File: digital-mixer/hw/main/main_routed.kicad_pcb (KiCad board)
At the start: 2 copper layers, 114 x 127.9 mm, 184 parts, among them J1 GCT USB4085, J10 MIDI OUT SJ-43514-SMT, J2 LiPo 1S 3000 mAh (з платою за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, J3 IN1 SJ-43514-SMT, J4 IN2 SJ-43514-SMT, J5 IN3 SJ-43514-SMT, J6 IN4 SJ-43514-SMT, J7 MAIN OUT SJ-43514-SMT, J8 AUX OUT SJ-43514-SMT, J9 PHONES SJ-43514-SMT, Q1 AO3401A, SW1 Power 7x7 DPDT self-lock, SW10 EC11 ch3.1, SW11 EC11 ch3.2, SW12 EC11 ch3.3, SW13 Mute 3 TSF-1266, SW14 EC11 ch4.1, SW15 EC11 ch4.2, SW16 EC11 ch4.3, SW17 Mute 4 TSF-1266, SW18 EC11 master, SW19 FX1 TSF-1266, SW2 EC11 ch1.1, SW20 FX2 TSF-1266, SW21 AUX TSF-1266, SW22 CUE TSF-1266, SW23 SHIFT TSF-1266, SW3 EC11 ch1.2, SW4 EC11 ch1.3, SW5 Mute 1 TSF-1266, SW6 EC11 ch2.1, SW7 EC11 ch2.2, SW8 EC11 ch2.3, SW9 Mute 2 TSF-1266, U1 Teensy 4.1, U10 PCM5102A, U11 TPA6132A2, U12 MCP23017-E/SO, U13 MCP23017-E/SO, U2 USBLC6-2SC6, U3 TP4056, U4 TPS63802, U5 LP5907MFX-3.3, U6 PCM1865, U7 PCM1865, U8 PCM5102A, U9 PCM5102A

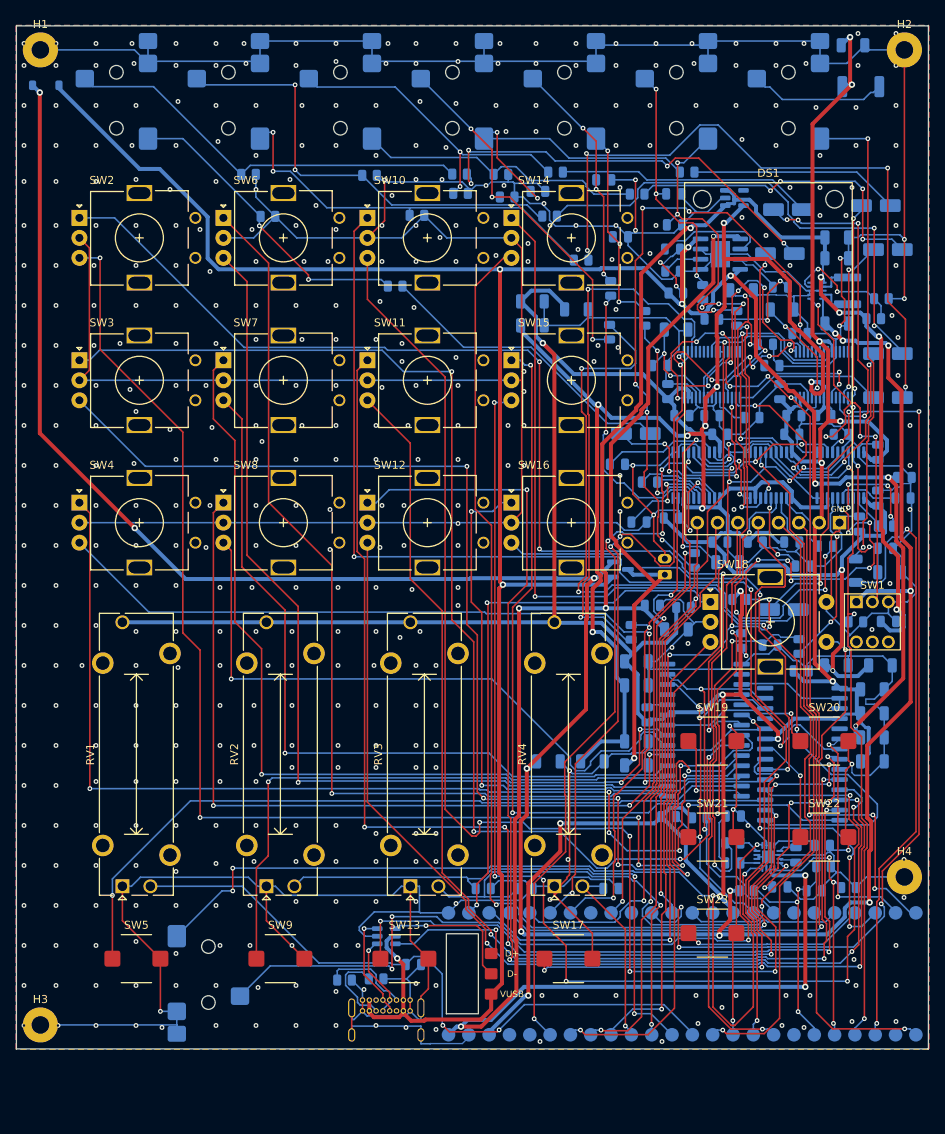
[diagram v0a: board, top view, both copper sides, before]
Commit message: digital-mixer: компоновка C (DM25-DM30), SMD-енкодери, USB4110, розводка 0 помилок
- компоновка C: колонки каналів на одних осях, ON / дисплей / MASTER в один ряд,
  Teensy у передньому правому куті, виходи на правому торці, M2 у чотирьох кутах
- EC12SY SMD з кнопками (DM26) + третій MCP23017; кнопку CUE прибрано (DM28)
- кнопка живлення 5,8 мм SMD (DM27), USB-C GCT USB4110 SMD (DM30), JST PH SMD
- 33 Ω на тактах I2S / TDM (DM29); такти 60-73 мм замість ~110
- 3D-моделі для всіх власних і стокових footprint без моделі (hw/lib/gen_3d.py)
- common: route_pcb --hole-keep, rip_near.py, параметри проєкту в kisch
- DRC: 0 порушень, 0 нез'єднаних, 0 розбіжностей зі схемою; ERC 0

Co-Authored-By: Claude Opus 5.5 <noreply@anthropic.com>
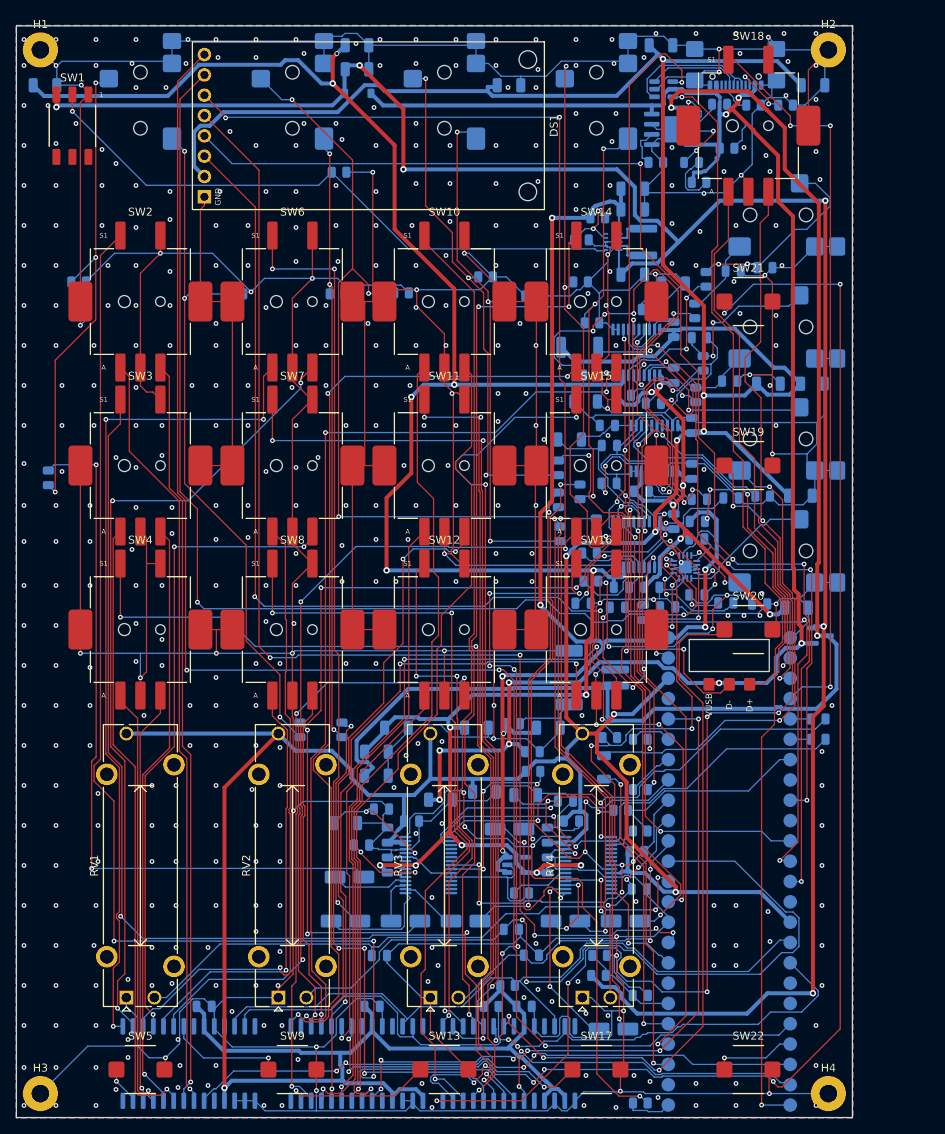
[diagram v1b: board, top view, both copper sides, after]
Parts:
- removed SW23: SHIFT TSF-1266, pocket-digital:SW_TSF-1266_6x6mm_SMD
- added C82: 10u, Capacitor_SMD:C_1206_3216Metric, B.Cu at (119.6, 27.4)
- added R44: 470, Resistor_SMD:R_0805_2012Metric, B.Cu at (105.8, 62.2)
- added R45: 470, Resistor_SMD:R_0805_2012Metric, B.Cu at (91.6, 85.9)
- added R46: 470, Resistor_SMD:R_0805_2012Metric, B.Cu at (91.8, 89.4)
- added R47: 33 0.5W, Resistor_SMD:R_2010_5025Metric, B.Cu at (90.4, 60.2)
- added R48: 10 0.25W, Resistor_SMD:R_1206_3216Metric, B.Cu at (93.4, 112.7)
- added U14: MCP23017-E/SO, Package_SO:SOIC-28W_7.5x17.9mm_P1.27mm, B.Cu at (81.6, 149.7)
- C81: value 10u -> 100n; footprint Capacitor_SMD:C_1206_3216Metric -> Capacitor_SMD:C_0805_2012Metric
- J1: value GCT USB4085 -> GCT USB4110-GF-A; footprint Connector_USB:USB_C_Receptacle_GCT_USB4085 -> Connector_USB:USB_C_Receptacle_GCT_USB4110
- J2: footprint Connector_JST:JST_PH_B2B-PH-K_1x02_P2.00mm_Vertical -> Connector_JST:JST_PH_S2B-PH-SM4-TB_1x02-1MP_P2.00mm_Horizontal
- R10: value 5.1k -> 10k
- R11: value 2.4k -> 10k
- R12, R13: value 1k -> 100k
- R14: value 100k -> 5.1k
- R15: value 665k -> 5.1k
- R16: value 91k -> 2.4k
- R17, R18: value 100k -> 1k
- R19, R23, R25, R32, R34: value 10k -> 100k
- R20: value 100k -> 665k
- R21: value 10k -> 91k
- R24, R33: value 100k -> 10k
- R26, R35: value 33 -> 10k
- R31, R7, R8: value 100k -> 33
- R36, R38: value 470 -> 100k
- R37, R39: value 470 -> 10k
- R40: value 470 -> 33
- R42: value 33 0.5W -> 470; footprint Resistor_SMD:R_2010_5025Metric -> Resistor_SMD:R_0805_2012Metric
- R43: value 10 0.25W -> 470; footprint Resistor_SMD:R_1206_3216Metric -> Resistor_SMD:R_0805_2012Metric
- R5, R6: value 10k -> 33
- R9: value 5.1k -> 33
- SW1: value Power 7x7 DPDT self-lock -> Power 5.8mm DPDT self-lock SMD; footprint pocket-digital:SW_Push_Latching_DPDT_7x7mm -> pocket-digital:SW_Push_Latching_DPDT_5.8mm_SMD
- SW10: value EC11 ch3.1 -> EC12SY ch3.1; footprint Rotary_Encoder:RotaryEncoder_Alps_EC11E_Vertical_H20mm -> pocket-digital:RotaryEncoder_EC12SY_SMD
- SW11: value EC11 ch3.2 -> EC12SY ch3.2; footprint Rotary_Encoder:RotaryEncoder_Alps_EC11E_Vertical_H20mm -> pocket-digital:RotaryEncoder_EC12SY_SMD
- SW12: value EC11 ch3.3 -> EC12SY ch3.3; footprint Rotary_Encoder:RotaryEncoder_Alps_EC11E_Vertical_H20mm -> pocket-digital:RotaryEncoder_EC12SY_SMD
- SW14: value EC11 ch4.1 -> EC12SY ch4.1; footprint Rotary_Encoder:RotaryEncoder_Alps_EC11E_Vertical_H20mm -> pocket-digital:RotaryEncoder_EC12SY_SMD
- SW15: value EC11 ch4.2 -> EC12SY ch4.2; footprint Rotary_Encoder:RotaryEncoder_Alps_EC11E_Vertical_H20mm -> pocket-digital:RotaryEncoder_EC12SY_SMD
- SW16: value EC11 ch4.3 -> EC12SY ch4.3; footprint Rotary_Encoder:RotaryEncoder_Alps_EC11E_Vertical_H20mm -> pocket-digital:RotaryEncoder_EC12SY_SMD
- SW18: value EC11 master -> EC12SY master; footprint Rotary_Encoder:RotaryEncoder_Alps_EC11E-Switch_Vertical_H20mm -> pocket-digital:RotaryEncoder_EC12SY_SMD
- SW2: value EC11 ch1.1 -> EC12SY ch1.1; footprint Rotary_Encoder:RotaryEncoder_Alps_EC11E_Vertical_H20mm -> pocket-digital:RotaryEncoder_EC12SY_SMD
- SW22: value CUE TSF-1266 -> SHIFT TSF-1266
- SW3: value EC11 ch1.2 -> EC12SY ch1.2; footprint Rotary_Encoder:RotaryEncoder_Alps_EC11E_Vertical_H20mm -> pocket-digital:RotaryEncoder_EC12SY_SMD
- SW4: value EC11 ch1.3 -> EC12SY ch1.3; footprint Rotary_Encoder:RotaryEncoder_Alps_EC11E_Vertical_H20mm -> pocket-digital:RotaryEncoder_EC12SY_SMD
- SW6: value EC11 ch2.1 -> EC12SY ch2.1; footprint Rotary_Encoder:RotaryEncoder_Alps_EC11E_Vertical_H20mm -> pocket-digital:RotaryEncoder_EC12SY_SMD
- SW7: value EC11 ch2.2 -> EC12SY ch2.2; footprint Rotary_Encoder:RotaryEncoder_Alps_EC11E_Vertical_H20mm -> pocket-digital:RotaryEncoder_EC12SY_SMD
- SW8: value EC11 ch2.3 -> EC12SY ch2.3; footprint Rotary_Encoder:RotaryEncoder_Alps_EC11E_Vertical_H20mm -> pocket-digital:RotaryEncoder_EC12SY_SMD
- moved J1 124.9 mm to (109.9, 23.7), turned to 0 degrees
- moved SW1 117.7 mm to (27.0, 32.5)
- moved U2 111.4 mm to (100.9, 27.9)
- moved C81 108.8 mm to (97.9, 127.9)
- moved J9 99.9 mm to (123.2, 85.6), turned to 180 degrees
- moved C13 94.7 mm to (61.6, 126.4)
- moved C52 94.2 mm to (62.6, 22.4)
- moved C14 94.2 mm to (61.1, 131.9)
- moved C24 93.1 mm to (88.6, 131.9)
- moved C25 91.2 mm to (96.1, 131.9)
- moved C26 90.4 mm to (81.6, 120.4)
- moved C6 89.8 mm to (62.6, 25.4)
- moved C15 88.4 mm to (76.1, 131.9)
- moved U5 87.7 mm to (82.5, 124.9)
- moved R13 83.3 mm to (92.9, 136.2)
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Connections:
- C77 pad 1: /FADER1 -> /+3V3
- C78 pad 1: /FADER2 -> /FADER1
- C79 pad 1: /FADER3 -> /FADER2
- C80 pad 1: /FADER4 -> /FADER3
- C81 pad 1: /+3V3 -> /FADER4
- R10 pad 1: /CC2 -> /DAC_XSMT
- R11 pad 1: /CHG_PROG -> /HP_EN
- R12 pad 1: /VBUS -> /VSYS
- R12 pad 2: /CHG_LED_RA -> /VBAT_SENSE
- R13 pad 1: /VBUS -> /VBAT_SENSE
- R13 pad 2: /CHG_LED_GA -> /GND
- R14 pad 1: /VBUS -> /CC1
- R15 pad 1: /+4V2 -> /CC2
- R15 pad 2: /BB_FB -> /GND
- R16 pad 1: /BB_FB -> /CHG_PROG
- R17 pad 1: /PWR_EN -> /VBUS
- R17 pad 2: /GND -> /CHG_LED_RA
- R18 pad 1: /IN1_T -> /VBUS
- R18 pad 2: /GND -> /CHG_LED_GA
- R19 pad 1: /IN1_T -> /VBUS
- R19 pad 2: /IN1_LS -> /GND
- R20 pad 1: /IN1_R -> /+4V2
- R20 pad 2: /GND -> /BB_FB
- R21 pad 1: /IN1_R -> /BB_FB
- R21 pad 2: /IN1_RS -> /GND
- R22 pad 1: /IN2_T -> /PWR_EN
- R23 pad 1: /IN2_T -> /IN1_T
- R23 pad 2: /IN2_LS -> /GND
- R24 pad 1: /IN2_R -> /IN1_T
- R24 pad 2: /GND -> /IN1_LS
- R25 pad 1: /IN2_R -> /IN1_R
- R25 pad 2: /IN2_RS -> /GND
- R26 pad 1: /ADC1_DOUT -> /IN1_R
- R26 pad 2: /ADC_DOUT -> /IN1_RS
- R27 pad 1: /IN3_T -> /IN2_T
- R28 pad 1: /IN3_T -> /IN2_T
- R28 pad 2: /IN3_LS -> /IN2_LS
- R29 pad 1: /IN3_R -> /IN2_R
- R30 pad 1: /IN3_R -> /IN2_R
- R30 pad 2: /IN3_RS -> /IN2_RS
- R31 pad 1: /IN4_T -> /ADC1_DOUT
- R31 pad 2: /GND -> /ADC_DOUT
- R32 pad 1: /IN4_T -> /IN3_T
- R32 pad 2: /IN4_LS -> /GND
- R33 pad 1: /IN4_R -> /IN3_T
- R33 pad 2: /GND -> /IN3_LS
- R34 pad 1: /IN4_R -> /IN3_R
- R34 pad 2: /IN4_RS -> /GND
- R35 pad 1: /ADC2_DOUT -> /IN3_R
- R35 pad 2: /ADC_DOUT -> /IN3_RS
- R36 pad 1: /MAIN_OL -> /IN4_T
- R36 pad 2: /MAIN_L -> /GND
- R37 pad 1: /MAIN_OR -> /IN4_T
- R37 pad 2: /MAIN_R -> /IN4_LS
- R38 pad 1: /AUX_OL -> /IN4_R
- R38 pad 2: /AUX_L -> /GND
- R39 pad 1: /AUX_OR -> /IN4_R
- R39 pad 2: /AUX_R -> /IN4_RS
- R40 pad 1: /CUE_OL -> /ADC2_DOUT
- R40 pad 2: /CUE_L -> /ADC_DOUT
- R41 pad 1: /CUE_OR -> /MAIN_OL
- R41 pad 2: /CUE_R -> /MAIN_L
- R42 pad 1: /+3V3 -> /MAIN_OR
- R42 pad 2: /MIDI_SRC -> /MAIN_R
- R43 pad 1: /MIDI_TX -> /AUX_OL
- R43 pad 2: /MIDI_SINK -> /AUX_L
- R5 pad 1: /DAC_XSMT -> /DAC_BCK_T
- R5 pad 2: /GND -> /DAC_BCK
- R6 pad 1: /HP_EN -> /DAC_LRCK_T
- R6 pad 2: /GND -> /DAC_LRCK
- R7 pad 1: /VSYS -> /ADC_BCK_T
- R7 pad 2: /VBAT_SENSE -> /ADC_BCK
- R8 pad 1: /VBAT_SENSE -> /ADC_LRCK_T
- R8 pad 2: /GND -> /ADC_LRCK
- R9 pad 1: /CC1 -> /ADC_MCLK_T
- R9 pad 2: /GND -> /ADC_MCLK
- SW1 pad 1: /VSYS -> /GND
- SW1 pad 3: /GND -> /VSYS
- SW10 pad MP: (no net) -> /GND
- SW11 pad MP: (no net) -> /GND
- SW12 pad MP: (no net) -> /GND
- SW14 pad MP: (no net) -> /GND
- SW15 pad MP: (no net) -> /GND
- SW16 pad MP: (no net) -> /GND
- SW18 pad MP: (no net) -> /GND
- SW2 pad MP: (no net) -> /GND
- SW22 pad 1: /BTN_CUE -> /BTN_SHIFT
- SW3 pad MP: (no net) -> /GND
- SW4 pad MP: (no net) -> /GND
- SW6 pad MP: (no net) -> /GND
- SW7 pad MP: (no net) -> /GND
- SW8 pad MP: (no net) -> /GND
- U1 pad 25: /ADC_MCLK -> /ADC_MCLK_T
- U1 pad 42: /DAC_LRCK -> /DAC_LRCK_T
- U1 pad 43: /DAC_BCK -> /DAC_BCK_T
- U1 pad 44: unconnected-(U1-22_A8_CTX1-Pad44) -> /MCP3_INT
- U1 pad 5: /ADC_LRCK -> /ADC_LRCK_T
- U1 pad 6: /ADC_BCK -> /ADC_BCK_T
- U12 pad 28: /BTN_FX1 -> unconnected-(U12-GPA7-Pad28)
- U12 pad 8: /BTN_FX2 -> unconnected-(U12-GPB7-Pad8)
- U13 pad 28: /BTN_AUX -> unconnected-(U13-GPA7-Pad28)
- U13 pad 8: /BTN_CUE -> unconnected-(U13-GPB7-Pad8)
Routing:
- net /GND: track 1298.9 -> 1709.0 mm, vias 450 -> 457
- net /ENC1_1_SW: track 0.00 -> 163.7 mm, vias 0 -> 3
- net /BTN_AUX: track 23.7 -> 173.9 mm, vias 1 -> 7
- net /+3V3: track 447.4 -> 584.5 mm, vias 13 -> 9
- net /ENC1_2_SW: track 0.00 -> 134.2 mm, vias 0 -> 3
- net /ENC2_1_SW: track 0.00 -> 133.9 mm, vias 0 -> 5
- net /LCD_CS: track 52.3 -> 179.8 mm, vias 1 -> 3
- net /LCD_BLK: track 77.3 -> 199.4 mm, vias 1 -> 3
- net /+4V2: track 278.5 -> 158.0 mm, vias 10 -> 7
- net /BTN_FX1: track 12.6 -> 132.8 mm, vias 1 -> 7
- net /ENC2_2_SW: track 0.00 -> 116.8 mm, vias 0 -> 3
- net /VBUS: track 328.2 -> 213.4 mm, vias 9 -> 8
- net /ENC4_1_SW: track 0.00 -> 113.2 mm, vias 0 -> 3
- net /ENC1_3_SW: track 0.00 -> 112.7 mm, vias 0 -> 3
- net /PH_L: track 114.4 -> 8.20 mm, vias 4 -> 2
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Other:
- board size 114 x 127.9 mm -> 104.5 x 136.5 mm

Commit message: digital-mixer: 4 шари (DM31), пара USB D+/D- наперед, розводка 0 помилок
- плата 4 шари як Rev A: F сигнали / In1 GND / In2 сигнали й живлення / B сигнали; доріжки 0,2 мм
- USB D+/D- прокладено парою 0,2/0,2 мм над In1 (92,5 / 90,9 мм) і зафіксовано до автороутера
- кнопки правої колонки повернуті площадкою GND до пари; конденсатори накачки й вихідні
  470 Ом ЦАП, конденсатори TPA6132A2 - біля виводів; TPA6132A2 розвернута до PHONES
- common: patch_route --ignore, fix_pcb --no-cleanup і переходи в острівці GND, кінці доріжок у
  переходах не вважаються висячими, виправлено падіння на видалених переходах
- DRC: 0 порушень, 0 нез'єднаних, 0 розбіжностей зі схемою; ERC 0

Co-Authored-By: Claude Opus 5.5 <noreply@anthropic.com>
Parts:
- moved C42 71.3 mm to (65.0, 110.7)
- moved C41 70.2 mm to (118.0, 64.7)
- moved C35 63.3 mm to (67.5, 107.7)
- moved C23 54.1 mm to (118.0, 78.7)
- moved Q1 44.9 mm to (89.0, 64.2)
- moved C11 41.8 mm to (89.5, 67.7)
- moved C18 39.5 mm to (81.0, 107.7)
- moved R10 27.3 mm to (88.8, 90.8)
- moved C66 24.5 mm to (112.7, 78.5)
- moved R44 20.6 mm to (92.5, 77.9)
- moved C10 20.0 mm to (98.0, 95.2)
- moved C68 19.8 mm to (93.1, 92.6)
- moved C55 17.6 mm to (108.7, 64.7)
- moved R41 16.6 mm to (93.2, 67.4)
- moved R42 15.8 mm to (92.8, 59.9)
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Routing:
- net /GND: track 1709.0 -> 627.8 mm, vias 457 -> 514
- net /VSYS: track 263.8 -> 205.1 mm, vias 6 -> 4
- net /FADER2: track 101.9 -> 56.1 mm
- net /BTN_AUX: track 173.9 -> 128.5 mm, vias 7 -> 3
- net /BAT+: track 169.8 -> 137.2 mm, vias 2 -> 5
- net /+4V2: track 158.0 -> 131.1 mm
- net /AUX_R: track 20.5 -> 47.2 mm
- net /CUE_CAPP: track 30.7 -> 4.27 mm, vias 4 -> 2
- net /+3V3: track 584.5 -> 561.3 mm, vias 9 -> 19
- net /MAIN_L: track 9.86 -> 32.6 mm, vias 0 -> 2
- net /CUE_CAPM: track 26.0 -> 3.39 mm, vias 2 -> 0
- net /AUX_L: track 7.36 -> 27.8 mm, vias 0 -> 2
- net /MAIN_R: track 24.9 -> 43.8 mm
- net /LCD_CS: track 179.8 -> 161.7 mm, vias 3 -> 2
- net /ENC3_3_B: track 75.4 -> 60.2 mm, vias 3 -> 1
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- added copper zone on In1.Cu, net /GND
- added copper zone on In2.Cu, net /GND
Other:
- copper layers 2 -> 4

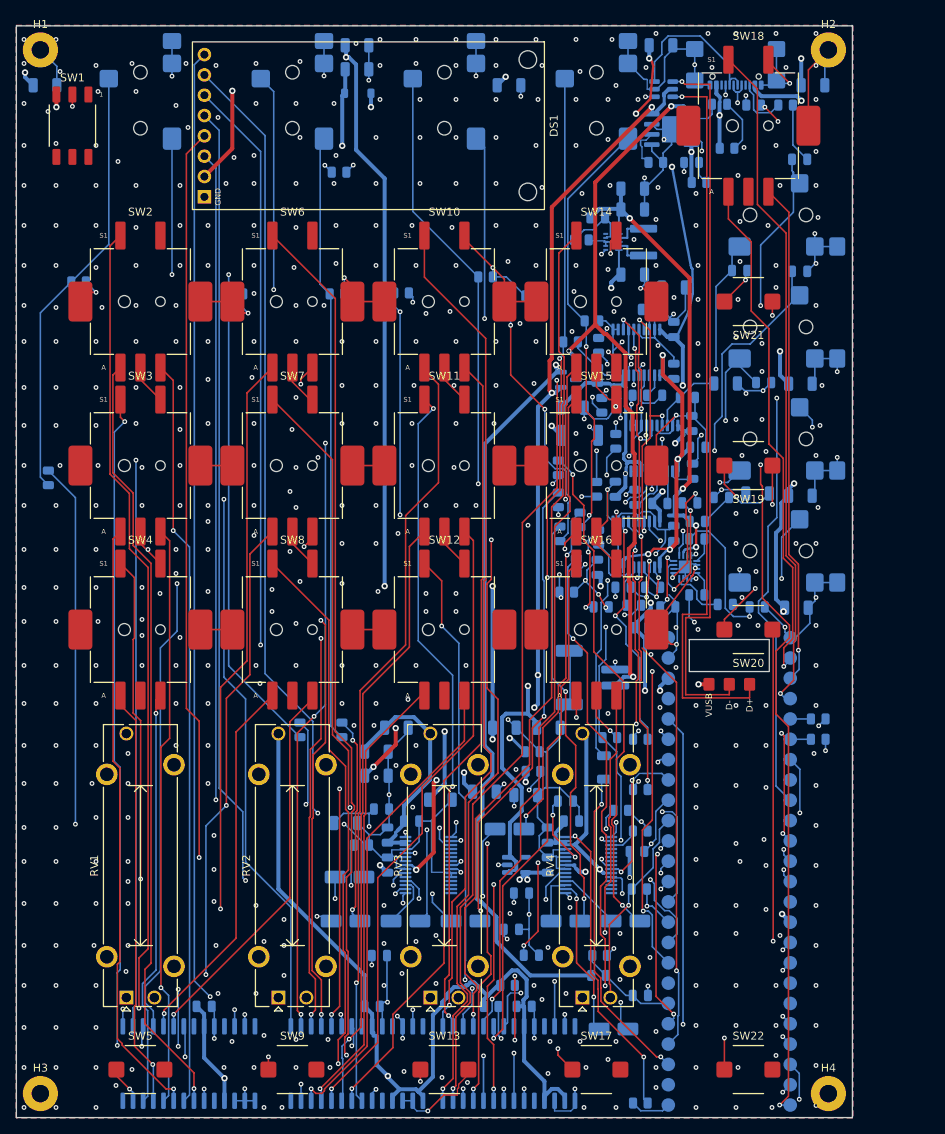
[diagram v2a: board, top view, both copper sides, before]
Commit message: digital-mixer: Teensy на гребінках з PSRAM (DM35), прошивка 0.2, GPL-3.0 (DM36)
Плата: Teensy 4.1 на гребінках у наскрізні отвори (зазор 2,5 мм під PSRAM),
D-/D+ теж наскрізні, Teensy за 6 мм від переднього краю, бокові джеки з кроком
12,5 мм, лапки EC12SY укорочено; перерозведено - DRC 0 порушень, 0 розривів.
Gerber, BOM і файли NextPCB оновлено.

Прошивка: метри каналів після фейдера (CLIP - лише вхід АЦП), калібрування
фейдерів, SHIFT HOLD/TOGGLE, MASTER = AUX у шарі AUX, кроки гучностей,
виправлено EQ на мінімумі, піктограма батареї, назви FX на екрані; збірка
uac2 (UAC2 8x8, 48 kHz) через tools/setup_uac2.sh.

Ліцензія digital-mixer/ - GPL-3.0-or-later.

Co-Authored-By: Claude Opus 5.5 <noreply@anthropic.com>
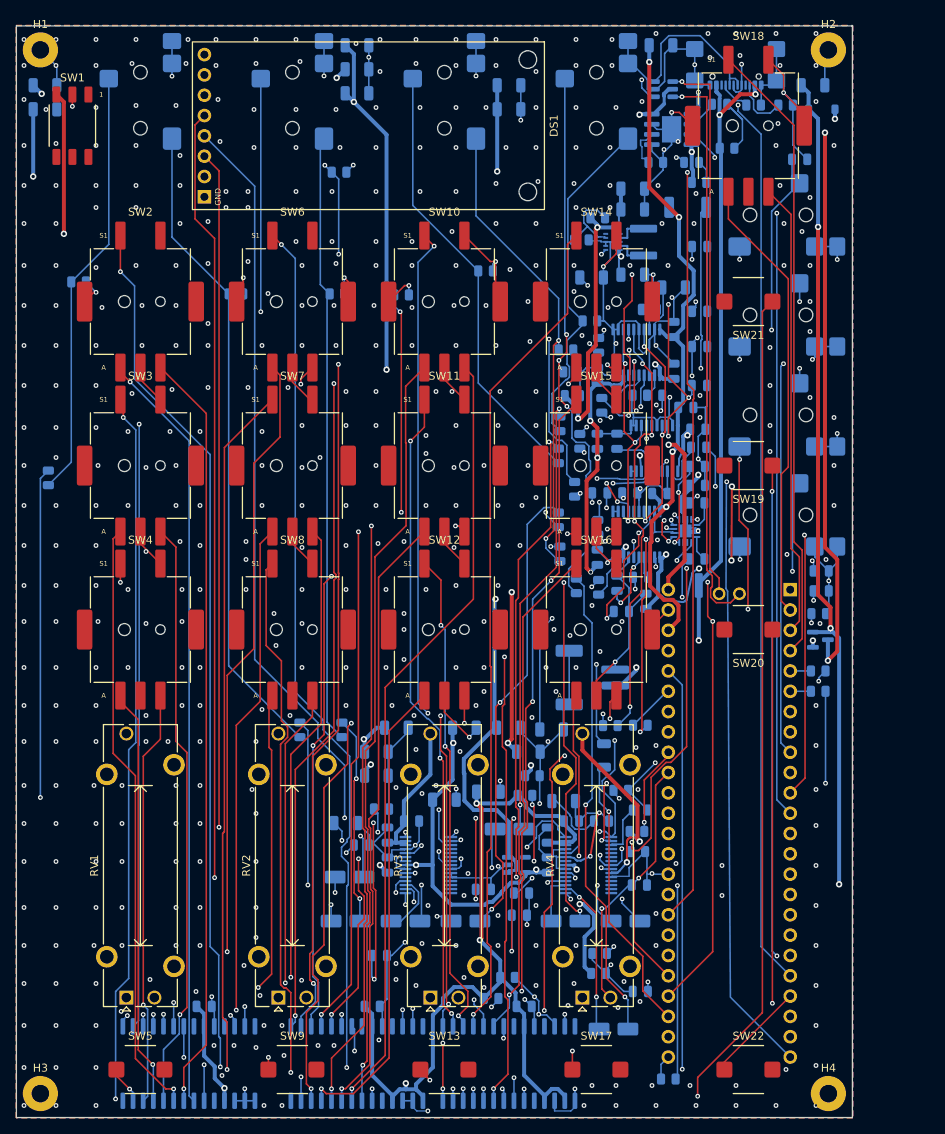
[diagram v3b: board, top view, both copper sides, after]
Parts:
- U1: footprint pocket-digital:Teensy41_SMD -> pocket-digital:Teensy41_THT
- moved C42 95.2 mm to (100.6, 22.4)
- moved C5 88.3 mm to (62.6, 25.4)
- moved C41 69.7 mm to (62.6, 22.4)
- moved C23 58.2 mm to (67.5, 107.7)
- moved C64 58.1 mm to (23.6, 30.4)
- moved D3 58.0 mm to (120.7, 30.4)
- moved C6 57.0 mm to (119.6, 27.4)
- moved Q1 45.3 mm to (120.5, 96.7)
- moved C2 44.8 mm to (79.0, 115.7)
- moved C11 43.4 mm to (84.0, 110.7)
- moved C52 39.3 mm to (23.6, 27.4)
- moved C66 39.2 mm to (86.9, 108.0)
- moved C63 39.0 mm to (62.6, 28.4)
- moved C82 38.1 mm to (81.6, 30.4)
- moved R10 31.6 mm to (120.3, 93.5)
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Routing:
- net /GND: track 627.8 -> 561.4 mm, vias 514 -> 496
- net /+3V3: track 561.3 -> 495.9 mm, vias 19 -> 13
- net /VSYS: track 205.1 -> 267.4 mm, vias 4 -> 6
- net /VBUS: track 217.4 -> 187.7 mm, vias 11 -> 9
- net /BAT+: track 137.2 -> 166.3 mm
- net /MAIN_VNEG: track 30.2 -> 4.26 mm, vias 2 -> 0
- net /AUX_LDOO: track 9.12 -> 34.1 mm, vias 0 -> 4
- net /USB_DN: track 90.9 -> 69.0 mm
- net /USB_DP: track 92.5 -> 71.5 mm
- net /CUE_LDOO: track 17.9 -> 38.3 mm, vias 2 -> 3
- net /+4V2: track 131.1 -> 150.8 mm, vias 7 -> 5
- net /LCD_MOSI: track 169.6 -> 150.1 mm, vias 2 -> 1
- net /FADER1: track 71.4 -> 90.5 mm
- net /LCD_BLK: track 195.8 -> 180.9 mm, vias 2 -> 1
- net /CUE_CAPP: track 4.27 -> 19.1 mm
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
